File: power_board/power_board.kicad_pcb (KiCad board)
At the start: 2 copper layers, 5 parts, among them Q1 IQD016N08NM5SCATMA1, Q2 IQD016N08NM5SCATMA1, U1 STM32L431KCUx, U2 UCC27282DRCR

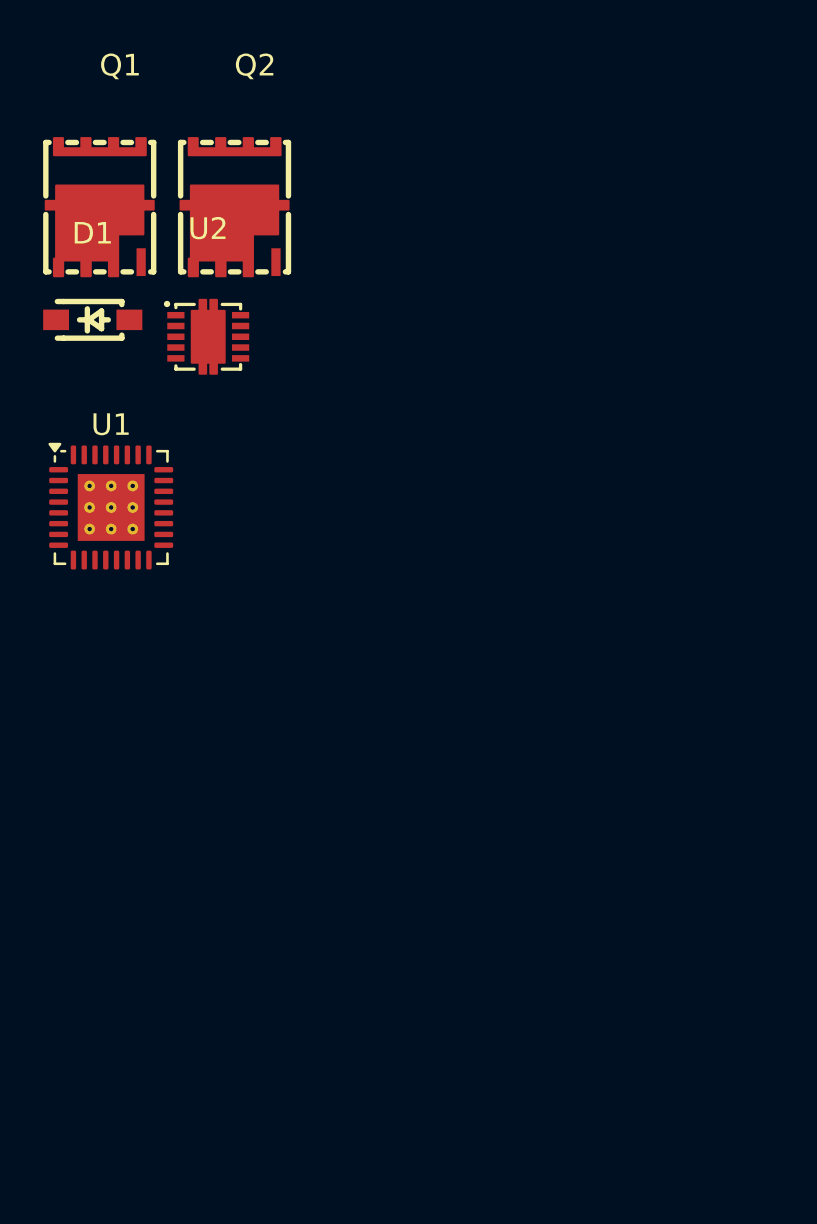
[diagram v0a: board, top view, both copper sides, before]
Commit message: Seperat submodules into split sheets
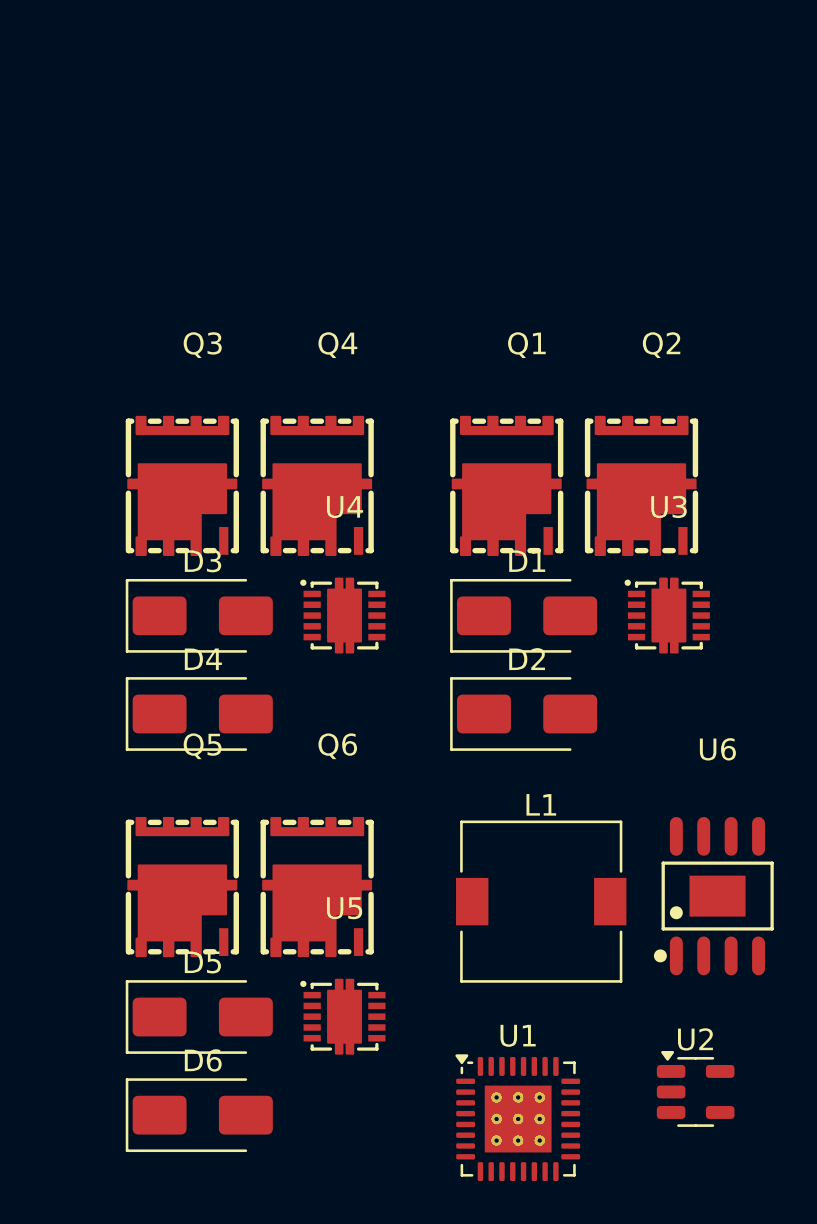
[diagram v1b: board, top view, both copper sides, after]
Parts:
- added D2: SS34, Diode_SMD:D_SMA, F.Cu at (69.5, 63.5)
- added D3: SS34, Diode_SMD:D_SMA, F.Cu at (54.5, 59.0)
- added D4: SS34, Diode_SMD:D_SMA, F.Cu at (54.5, 63.5)
- added D5: SS34, Diode_SMD:D_SMA, F.Cu at (54.5, 77.6)
- added D6: SS34, Diode_SMD:D_SMA, F.Cu at (54.5, 82.1)
- added L1: L_Small, Inductor_SMD:L_7.3x7.3_H4.5, F.Cu at (70.2, 72.2)
- added Q3: IQD016N08NM5SCATMA1, esc-library:PG-TSON-8_L6.0-W5.0_IQD020N10NM5ATMA1, F.Cu at (54.5, 52.9)
- added Q4: IQD016N08NM5SCATMA1, esc-library:PG-TSON-8_L6.0-W5.0_IQD020N10NM5ATMA1, F.Cu at (60.8, 52.9)
- added Q5: IQD016N08NM5SCATMA1, esc-library:PG-TSON-8_L6.0-W5.0_IQD020N10NM5ATMA1, F.Cu at (54.5, 71.5)
- added Q6: IQD016N08NM5SCATMA1, esc-library:PG-TSON-8_L6.0-W5.0_IQD020N10NM5ATMA1, F.Cu at (60.8, 71.5)
- added U3: UCC27282DRCR, esc-library:VSON-10_L3.0-W3.0-P0.50-TL-EP, F.Cu at (76.1, 59.0)
- added U4: UCC27282DRCR, esc-library:VSON-10_L3.0-W3.0-P0.50-TL-EP, F.Cu at (61.1, 59.0)
- added U5: UCC27282DRCR, esc-library:VSON-10_L3.0-W3.0-P0.50-TL-EP, F.Cu at (61.1, 77.6)
- added U6: LM5163DDAR, esc-library:ESOP-8_L4.9-W3.9-P1.27-LS6.0-BL-EP2.6, F.Cu at (78.4, 72.0)
- D1: value BAV19W_C5204748 -> SS34; footprint esc-library:SOD-123_L2.7-W1.6-LS3.7-RD-1 -> Diode_SMD:D_SMA
- U2: value UCC27282DRCR -> INA180A1; footprint esc-library:VSON-10_L3.0-W3.0-P0.50-TL-EP -> Package_TO_SOT_SMD:SOT-23-5
- moved U2 41.7 mm to (77.4, 81.0)
- moved U1 34.1 mm to (69.1, 82.3)
- moved D1 24.4 mm to (69.5, 59.0)
- moved Q1 22.9 mm to (69.6, 52.9)
- moved Q2 22.9 mm to (75.8, 52.9)
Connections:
- net /MOTOR_PHASE_A renamed /half_bridge_0/MOTOR_PHASE
- net /half_bridge0/V_B renamed Net-(D1-K)
- net VBUS renamed /half_bridge_0/VDD
- D1 pad 2: /half_bridge0/VCC -> Net-(D1-A)
- Q1 pad 4: Net-(Q1-G) -> Net-(D1-A)
- Q2 pad 1: GND -> /curret_sense/current+
- U1 pad 1: unconnected-(U1-VDD-Pad1) -> +3V3
- U1 pad 10: unconnected-(U1-PA4-Pad10) -> /mcu/MOTOR_PHASE_FB_B
- U1 pad 11: unconnected-(U1-PA5-Pad11) -> /mcu/MOTOR_PHASE_FB_C
- U1 pad 12: unconnected-(U1-PA6-Pad12) -> /mcu/V_SENSE
- U1 pad 13: unconnected-(U1-PA7-Pad13) -> /half_bridge_2/DRIVER_LOW
- U1 pad 14: unconnected-(U1-PB0-Pad14) -> /half_bridge_1/DRIVER_LOW
- U1 pad 15: unconnected-(U1-PB1-Pad15) -> /half_bridge_0/DRIVER_LOW
- U1 pad 16: Net-(U1-VSS-Pad16) -> GND
- U1 pad 17: unconnected-(U1-VDD-Pad17) -> +3V3
- U1 pad 18: unconnected-(U1-PA8-Pad18) -> /half_bridge_2/DRIVER_HIGH
- U1 pad 19: unconnected-(U1-PA9-Pad19) -> /half_bridge_1/DRIVER_HIGH
- U1 pad 20: unconnected-(U1-PA10-Pad20) -> /half_bridge_0/DRIVER_HIGH
- U1 pad 23: unconnected-(U1-PA13-Pad23) -> /mcu/SWDIO
- U1 pad 24: unconnected-(U1-PA14-Pad24) -> /mcu/SWDCLK
- U1 pad 32: Net-(U1-VSS-Pad16) -> GND
- U1 pad 33: Net-(U1-VSS-Pad16) -> GND
- U1 pad 5: unconnected-(U1-VDDA-Pad5) -> +3V3A
- U1 pad 6: unconnected-(U1-PA0-Pad6) -> /mcu/MOTOR_PHASE_FB_A
- U1 pad 7: unconnected-(U1-PA1-Pad7) -> /mcu/BEMF_REF
- U1 pad 9: unconnected-(U1-PA3-Pad9) -> /curret_sense/I_OUT
- U2 pad 1: unconnected-(U2-VDD-Pad1) -> Net-(R8-Pad1)
- U2 pad 2: unconnected-(U2-NC-Pad2) -> GND
- U2 pad 3: unconnected-(U2-HB-Pad3) -> /curret_sense/current+
- U2 pad 4: unconnected-(U2-HO-Pad4) -> /curret_sense/current-
- U2 pad 5: unconnected-(U2-HS-Pad5) -> +3V3

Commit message: Start multichannel layout
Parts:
- removed U1: STM32L431KCUx, Package_DFN_QFN:QFN-32-1EP_5x5mm_P0.5mm_EP3.1x3.1mm_ThermalVias
- removed U2: INA180A1, Package_TO_SOT_SMD:SOT-23-5
- added C1: 10u, Capacitor_SMD:C_2220_5750Metric, F.Cu at (25.6, 23.7)
- added C10: 100n, Capacitor_SMD:C_0603_1608Metric, F.Cu at (38.4, 69.2)
- added C11: 100n, Capacitor_SMD:C_0603_1608Metric, F.Cu at (42.4, 101.3)
- added C12: 100n, Capacitor_SMD:C_0603_1608Metric, F.Cu at (42.4, 103.8)
- added C13: 1u, Capacitor_SMD:C_0603_1608Metric, F.Cu at (159.4, 81.8)
- added C14: 100n, Capacitor_SMD:C_0603_1608Metric, F.Cu at (159.2, 79.3)
- added C15: 100n, Capacitor_SMD:C_0603_1608Metric, F.Cu at (156.0, 79.3)
- added C16: 1000p, Capacitor_SMD:C_0603_1608Metric, F.Cu at (156.0, 77.7)
- added C17: 1u, Capacitor_SMD:C_0603_1608Metric, F.Cu at (142.7, 81.8)
- added C18: 100n, Capacitor_SMD:C_0603_1608Metric, F.Cu at (142.5, 79.3)
- added C19: 100n, Capacitor_SMD:C_0603_1608Metric, F.Cu at (139.3, 77.7)
- added C2: 10u, Capacitor_SMD:C_2220_5750Metric, F.Cu at (25.6, 30.6)
- added C20: 1000p, Capacitor_SMD:C_0603_1608Metric, F.Cu at (139.3, 79.3)
- added C21: 1u, Capacitor_SMD:C_0603_1608Metric, F.Cu at (175.6, 79.1)
- added C22: 100n, Capacitor_SMD:C_0603_1608Metric, F.Cu at (175.8, 81.6)
- added C23: 100n, Capacitor_SMD:C_0603_1608Metric, F.Cu at (172.4, 77.5)
- added C24: 1000p, Capacitor_SMD:C_0603_1608Metric, F.Cu at (172.4, 79.1)
- added C25: 2.2u, Capacitor_SMD:C_0603_1608Metric, F.Cu at (66.2, 157.8)
- added C26: 1u, Capacitor_SMD:C_0603_1608Metric, F.Cu at (33.3, 138.6)
- added C27: 1u, Capacitor_SMD:C_0603_1608Metric, F.Cu at (32.0, 162.2)
- added C28: 1u, Capacitor_SMD:C_0603_1608Metric, F.Cu at (38.9, 139.0)
- added C29: 1u, Capacitor_SMD:C_0603_1608Metric, F.Cu at (36.6, 160.0)
- added C3: 10u, Capacitor_SMD:C_2220_5750Metric, F.Cu at (25.6, 37.6)
- added C30: 2.2u, Capacitor_SMD:C_0603_1608Metric, F.Cu at (109.1, 154.9)
- added C31: 56p, Capacitor_SMD:C_0603_1608Metric, F.Cu at (83.2, 161.9)
- added C32: 10n, Capacitor_SMD:C_0603_1608Metric, F.Cu at (47.9, 139.3)
- added C33: 10n, Capacitor_SMD:C_0603_1608Metric, F.Cu at (46.5, 166.8)
- added C34: 3.3n, Capacitor_SMD:C_0603_1608Metric, F.Cu at (83.2, 164.4)
- added C35: 22u, Capacitor_SMD:C_0603_1608Metric, F.Cu at (109.1, 162.4)
- added C36: 2.2u, Capacitor_SMD:C_0603_1608Metric, F.Cu at (47.9, 141.8)
- added C37: 2.2u, Capacitor_SMD:C_0603_1608Metric, F.Cu at (47.9, 163.2)
- added C4: 10u, Capacitor_SMD:C_2220_5750Metric, F.Cu at (25.6, 44.5)
- added C5: 100n, Capacitor_SMD:C_0603_1608Metric, F.Cu at (38.4, 66.2)
- added C6: 100n, Capacitor_SMD:C_0603_1608Metric, F.Cu at (38.4, 70.8)
- added C7: 100n, Capacitor_SMD:C_0603_1608Metric, F.Cu at (38.4, 67.7)
- added C8: 10u, Capacitor_SMD:C_0603_1608Metric, F.Cu at (38.4, 72.4)
- added C9: 100n, Capacitor_SMD:C_0603_1608Metric, F.Cu at (49.4, 72.4)
- added D7: LED, LED_SMD:LED_0603_1608Metric, F.Cu at (99.6, 161.4)
- added R1: 1k, Resistor_SMD:R_0603_1608Metric, F.Cu at (45.0, 64.1)
- added R10: 4.7, Resistor_SMD:R_0603_1608Metric, F.Cu at (156.8, 86.6)
- added R11: 4.7, Resistor_SMD:R_0603_1608Metric, F.Cu at (157.0, 75.0)
- added R12: 10, Resistor_SMD:R_0603_1608Metric, F.Cu at (155.0, 86.6)
- added R13: 10, Resistor_SMD:R_0603_1608Metric, F.Cu at (155.4, 75.0)
- added R14: 100k, Resistor_SMD:R_0603_1608Metric, F.Cu at (154.8, 91.4)
- added R15: 100k, Resistor_SMD:R_0603_1608Metric, F.Cu at (155.0, 71.6)
- added R16: 10k, Resistor_SMD:R_0603_1608Metric, F.Cu at (147.4, 85.2)
- added R17: 1k, Resistor_SMD:R_0603_1608Metric, F.Cu at (147.4, 89.2)
- added R18: 4.7, Resistor_SMD:R_0603_1608Metric, F.Cu at (140.1, 86.6)
- added R19: 4.7, Resistor_SMD:R_0603_1608Metric, F.Cu at (140.3, 75.0)
- added R2: 10k, Resistor_SMD:R_0603_1608Metric, F.Cu at (42.5, 64.1)
- added R20: 10, Resistor_SMD:R_0603_1608Metric, F.Cu at (138.3, 86.6)
- added R21: 10, Resistor_SMD:R_0603_1608Metric, F.Cu at (138.7, 75.0)
- added R22: 100k, Resistor_SMD:R_0603_1608Metric, F.Cu at (138.1, 91.4)
- added R23: 100k, Resistor_SMD:R_0603_1608Metric, F.Cu at (138.3, 71.6)
- added R24: 10k, Resistor_SMD:R_0603_1608Metric, F.Cu at (130.7, 85.2)
- added R25: 1k, Resistor_SMD:R_0603_1608Metric, F.Cu at (130.7, 89.2)
- added R26: 4.7, Resistor_SMD:R_0603_1608Metric, F.Cu at (173.2, 86.4)
- added R27: 4.7, Resistor_SMD:R_0603_1608Metric, F.Cu at (173.4, 74.8)
- added R28: 10, Resistor_SMD:R_0603_1608Metric, F.Cu at (171.4, 86.4)
- added R29: 10, Resistor_SMD:R_0603_1608Metric, F.Cu at (171.8, 74.8)
- added R3: 100k, Resistor_SMD:R_0603_1608Metric, F.Cu at (27.5, 79.5)
- added R30: 100k, Resistor_SMD:R_0603_1608Metric, F.Cu at (171.2, 91.2)
- added R31: 100k, Resistor_SMD:R_0603_1608Metric, F.Cu at (171.4, 71.4)
- added R32: 10k, Resistor_SMD:R_0603_1608Metric, F.Cu at (163.8, 85.0)
- added R33: 1k, Resistor_SMD:R_0603_1608Metric, F.Cu at (163.8, 89.0)
- added R34: 2.2, Resistor_SMD:R_0603_1608Metric, F.Cu at (33.2, 140.4)
- added R35: 1, Resistor_SMD:R_0603_1608Metric, F.Cu at (31.4, 159.8)
- added R36: R_Small, Resistor_SMD:R_0603_1608Metric, F.Cu at (66.2, 161.6)
- added R37: 226k, Resistor_SMD:R_0603_1608Metric, F.Cu at (87.2, 162.4)
- added R38: 453k, Resistor_SMD:R_0603_1608Metric, F.Cu at (78.5, 162.0)
- added R39: 49.9, Resistor_SMD:R_0603_1608Metric, F.Cu at (78.5, 164.5)
- added R4: 5k, Resistor_SMD:R_0603_1608Metric, F.Cu at (27.5, 82.0)
- added R40: 2.2k, Resistor_SMD:R_0603_1608Metric, F.Cu at (95.4, 162.3)
- added R5: 10k, Resistor_SMD:R_0603_1608Metric, F.Cu at (36.5, 80.0)
- added R6: 10k, Resistor_SMD:R_0603_1608Metric, F.Cu at (36.5, 82.5)
- added R7: 10k, Resistor_SMD:R_0603_1608Metric, F.Cu at (36.5, 85.5)
- added R8: 0.001, Resistor_SMD:R_0603_1608Metric, F.Cu at (42.4, 106.3)
- added R9: 1k, Resistor_SMD:R_0603_1608Metric, F.Cu at (42.4, 108.8)
- added U10: 66565S0M3, esc-library:CONN-SMD_66565S0M3, F.Cu at (166.8, 77.8)
- added U11: LM5163DDAR, esc-library:ESOP-8_L4.9-W3.9-P1.27-LS6.0-BL-EP2.6, F.Cu at (72.9, 157.8)
- added U12: LP2985-33DBVR, esc-library:SOT-23-5_L3.0-W1.7-P0.95-LS2.8-BR, F.Cu at (42.8, 139.3)
- added U13: LP2985-33DBVR, esc-library:SOT-23-5_L3.0-W1.7-P0.95-LS2.8-BR, F.Cu at (42.4, 160.7)
- added U7: UCC27282DRCR, esc-library:VSON-10_L3.0-W3.0-P0.50-TL-EP, F.Cu at (139.9, 82.5)
- added U8: 66565S0M3, esc-library:CONN-SMD_66565S0M3, F.Cu at (133.7, 78.0)
- added U9: UCC27282DRCR, esc-library:VSON-10_L3.0-W3.0-P0.50-TL-EP, F.Cu at (173.0, 82.3)
- D1, D2, D3, D4, D5, D6: value SS34 -> B5819WS_C7420331; footprint Diode_SMD:D_SMA -> esc-library:SOD-323_L1.7-W1.3-LS2.5-FD
- Q1, Q2, Q3, Q4, Q5, Q6: value IQD016N08NM5SCATMA1 -> BSC0702LS; footprint esc-library:PG-TSON-8_L6.0-W5.0_IQD020N10NM5ATMA1 -> esc-library:PG-TDSON-8_L5.0-W6.0-P1.27-BL-EP
- U3: value UCC27282DRCR -> STM32L431KCUx; footprint esc-library:VSON-10_L3.0-W3.0-P0.50-TL-EP -> Package_DFN_QFN:QFN-32-1EP_5x5mm_P0.5mm_EP3.1x3.1mm_ThermalVias
- U4: value UCC27282DRCR -> INA180A1; footprint esc-library:VSON-10_L3.0-W3.0-P0.50-TL-EP -> Package_TO_SOT_SMD:SOT-23-5
- U6: value LM5163DDAR -> 66565S0M3; footprint esc-library:ESOP-8_L4.9-W3.9-P1.27-LS6.0-BL-EP2.6 -> esc-library:CONN-SMD_66565S0M3
- moved D6 119.4 mm to (173.4, 71.4), turned to -90 degrees
- moved D5 119.3 mm to (173.2, 89.6), turned to 90 degrees
- moved Q5 112.4 mm to (166.9, 67.6)
- moved Q6 108.1 mm to (167.7, 87.6)
- moved U5 95.6 mm to (156.6, 82.5), turned to -90 degrees
- moved D1 92.5 mm to (156.8, 89.8), turned to 90 degrees
- moved D3 91.0 mm to (140.1, 89.8), turned to 90 degrees
- moved D2 87.8 mm to (157.0, 71.6), turned to -90 degrees
- moved D4 86.2 mm to (140.3, 71.6), turned to -90 degrees
- moved Q2 83.1 mm to (151.3, 87.8)
- moved Q1 82.3 mm to (150.5, 67.8)
- moved Q4 81.6 mm to (134.6, 87.8)
- moved Q3 80.6 mm to (133.8, 67.8)
- moved L1 79.0 mm to (85.0, 149.8)
- moved U6 72.3 mm to (150.4, 78.0), turned to 90 degrees
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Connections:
- D1 pad 1: Net-(D1-K) -> Net-(D1-A)
- D1 pad 2: Net-(D1-A) -> Net-(D1-K)
- D2 pad 1: Net-(D2-K) -> Net-(D2-A)
- D2 pad 2: Net-(D2-A) -> Net-(D2-K)
- D3 pad 1: Net-(D3-K) -> Net-(D3-A)
- D3 pad 2: Net-(D3-A) -> Net-(D3-K)
- D4 pad 1: Net-(D4-K) -> Net-(D4-A)
- D4 pad 2: Net-(D4-A) -> Net-(D4-K)
- D5 pad 1: Net-(D5-K) -> Net-(D5-A)
- D5 pad 2: Net-(D5-A) -> Net-(D5-K)
- D6 pad 1: Net-(D6-K) -> Net-(D6-A)
- D6 pad 2: Net-(D6-A) -> Net-(D6-K)
- L1 pad 1: Net-(U6-BST) -> Net-(U11-BST)
- Q1 pad 4: Net-(D1-A) -> Net-(D2-A)
- Q1 pad 5: /half_bridge_0/VDD -> VBUS
- Q2 pad 4: Net-(D2-A) -> Net-(D1-A)
- Q3 pad 4: Net-(D3-A) -> Net-(D4-A)
- Q3 pad 5: /half_bridge_1/VDD -> VBUS
- Q4 pad 4: Net-(D4-A) -> Net-(D3-A)
- Q5 pad 4: Net-(D5-A) -> Net-(D6-A)
- Q5 pad 5: /half_bridge_2/VDD -> VBUS
- Q6 pad 4: Net-(D6-A) -> Net-(D5-A)
- U3 pad 1: +12V -> +3V3
- U3 pad 10: /half_bridge_0/DRIVER_LO -> /mcu/MOTOR_PHASE_FB_B
- U3 pad 11: GNDPWR -> /mcu/MOTOR_PHASE_FB_C
- U3 pad 3: Net-(U3-HB) -> unconnected-(U3-PC15-Pad3)
- U3 pad 4: /half_bridge_0/DRIVER_HO -> Net-(U3-NRST)
- U3 pad 5: /half_bridge_0/MOTOR_PHASE -> +3V3A
- U3 pad 6: Net-(U3-EN) -> /mcu/MOTOR_PHASE_FB_A
- U3 pad 7: /half_bridge_0/DRIVER_HIGH -> /mcu/BEMF_REF
- U3 pad 8: /half_bridge_0/DRIVER_LOW -> unconnected-(U3-PA2-Pad8)
- U3 pad 9: GNDPWR -> /curret_sense/I_OUT
- U4 pad 1: +12V -> Net-(R9-Pad1)
- U4 pad 2: unconnected-(U4-NC-Pad2) -> GND
- U4 pad 3: Net-(U4-HB) -> /curret_sense/current+
- U4 pad 4: /half_bridge_1/DRIVER_HO -> GNDPWR
- U4 pad 5: /half_bridge_1/MOTOR_PHASE -> +3V3A
- U5 pad 10: /half_bridge_2/DRIVER_LO -> /half_bridge_0/DRIVER_LO
- U5 pad 4: /half_bridge_2/DRIVER_HO -> /half_bridge_0/DRIVER_HO
- U5 pad 5: /half_bridge_2/MOTOR_PHASE -> /half_bridge_0/MOTOR_PHASE
- U5 pad 6: Net-(U5-EN) -> +12V
- U5 pad 7: /half_bridge_2/DRIVER_HIGH -> /half_bridge_0/DRIVER_HIGH
- U5 pad 8: /half_bridge_2/DRIVER_LOW -> /half_bridge_0/DRIVER_LOW
- U6 pad 1: GND -> /half_bridge_0/MOTOR_PHASE
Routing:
- net GNDPWR: track 0.00 -> 43.2 mm, vias 0 -> 18
- net +12V: track 0.00 -> 12.8 mm, vias 0 -> 3
- net /curret_sense/current+: track 0.00 -> 11.1 mm
- net /half_bridge_1/MOTOR_PHASE: track 0.00 -> 8.66 mm
- net /half_bridge_0/MOTOR_PHASE: track 0.00 -> 8.66 mm
- net /half_bridge_2/MOTOR_PHASE: track 0.00 -> 8.66 mm
- net Net-(D4-A): track 0.00 -> 8.59 mm
- net Net-(D2-A): track 0.00 -> 8.59 mm
- net Net-(D6-A): track 0.00 -> 8.59 mm
- net /half_bridge_1/DRIVER_HO: track 0.00 -> 7.09 mm
- net /half_bridge_0/DRIVER_HO: track 0.00 -> 7.09 mm
- net /half_bridge_2/DRIVER_HO: track 0.00 -> 7.09 mm
- net Net-(D1-A): track 0.00 -> 6.97 mm
- net Net-(D5-A): track 0.00 -> 6.97 mm
- net Net-(D3-A): track 0.00 -> 6.97 mm
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- added copper zone on F.Cu, net /half_bridge_2/MOTOR_PHASE

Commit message: Complete primary layout step
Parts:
- removed the C1 at (25.6, 23.7)
- removed the C2 at (25.6, 30.6)
- removed the C3 at (25.6, 37.6)
- removed the C4 at (25.6, 44.5)
- added C13: 10u, Capacitor_SMD:C_1210_3225Metric, F.Cu at (60.3, 52.8)
- added C18: 10u, Capacitor_SMD:C_1210_3225Metric, F.Cu at (80.5, 52.8)
- added C23: 10u, Capacitor_SMD:C_1210_3225Metric, F.Cu at (100.7, 52.7)
- added C37: ERS1KM101G16OT, esc-library:CAP-TH_BD10.0-P5.00-D1.0-FD, F.Cu at (49.0, 54.8)
- added C38: ERS1KM101G16OT, esc-library:CAP-TH_BD10.0-P5.00-D1.0-FD, F.Cu at (49.1, 66.8)
- added C39: 1u, Capacitor_SMD:C_0603_1608Metric, F.Cu at (35.4, 99.8)
- added C40: 1u, Capacitor_SMD:C_0603_1608Metric, F.Cu at (39.4, 99.8)
- added C41: 10n, Capacitor_SMD:C_0603_1608Metric, F.Cu at (28.2, 98.6)
- added C42: 2.2u, Capacitor_SMD:C_0603_1608Metric, F.Cu at (28.2, 100.6)
- added CN1: XT90PW-M.G.Y, esc-library:CONN-TH_XT90PW-M.G.Y, F.Cu at (40.5, 32.3)
- added CN2: XT60PW-M, esc-library:CONN-TH_XT60PW-M, F.Cu at (33.8, 32.3)
- added R41: 2.2, Resistor_SMD:R_0603_1608Metric, F.Cu at (42.0, 101.0)
- added U12: LP2985-33DBVR, esc-library:SOT-23-5_L3.0-W1.7-P0.95-LS2.8-BR, F.Cu at (32.1, 99.6)
- C34: renamed from C35; footprint Capacitor_SMD:C_0603_1608Metric -> Capacitor_SMD:C_1210_3225Metric
- R36: value R_Small -> 100k
- R39: value 49.9 -> 49.9k
- R8: value 0.001 -> HOVB4026-5W-0.5MR-1%; footprint Resistor_SMD:R_0603_1608Metric -> esc-library:RES-SMD_4P-L10.8-W6.7
- moved C34 96.8 mm to (56.6, 81.0), turned to 180 degrees
- moved C29 87.5 mm to (52.4, 88.2), turned to 180 degrees
- moved C9 86.1 mm to (75.0, 64.4)
- moved D1 86.1 mm to (72.4, 72.4)
- moved Q1 86.1 mm to (66.1, 50.3)
- moved R10 86.1 mm to (72.4, 69.2)
- moved R13 86.1 mm to (71.0, 57.5)
- moved R14 86.1 mm to (70.4, 74.0)
- moved R16 86.1 mm to (63.0, 67.7)
- moved R17 86.1 mm to (63.0, 71.8)
- moved U4 86.1 mm to (66.0, 60.5)
- moved C10 86.1 mm to (74.8, 61.8)
- moved C11 86.1 mm to (71.6, 61.8)
- moved C12 86.1 mm to (71.6, 60.2)
- moved D2 86.1 mm to (72.6, 54.2)
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- renumbered C5 to C1, C14 to C10, C15 to C11, C16 to C12, C17 to C14, C18 to C15, C19 to C16, C20 to C17, C21 to C19, C6 to C2, C22 to C20, C23 to C21, C24 to C22, C25 to C24, C26 to C25, C27 to C26, C28 to C27, C29 to C28, C30 to C29, C7 to C3, C31 to C30, C32 to C31, C33 to C32, C34 to C33, C36 to C35, C37 to C36, C8 to C4, C9 to C5, C10 to C6, C11 to C7, C12 to C8, C13 to C9, U3 to U1, U12 to U10, U13 to U11, U4 to U2, U5 to U3, U6 to U4, U7 to U5, U8 to U6, U9 to U7, U10 to U8, U11 to U9
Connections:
- C29 pad 1: Net-(U11-SW) -> Net-(U9-SW)
- C29 pad 2: Net-(U11-BST) -> Net-(U9-BST)
- C7 pad 1: +3V3A -> +3V3A0
- L1 pad 1: Net-(U11-BST) -> Net-(U9-SW)
- R37 pad 2: Net-(U11-BST) -> Net-(U9-SW)
- R8 pad 1: /curret_sense/current+ -> GNDPWR
- R8 pad 2: GNDPWR -> /curret_sense/current+
- U2 pad 3: /curret_sense/current+ -> Net-(U2-+)
- U2 pad 4: GNDPWR -> Net-(U2--)
- U2 pad 5: +3V3A -> +3V3A0
- U9 pad 7: Net-(U11-BST) -> Net-(U9-BST)
- U9 pad 8: Net-(U11-SW) -> Net-(U9-SW)
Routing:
- added copper zone on F.Cu, net /half_bridge_0/MOTOR_PHASE
- added copper zone on F.Cu, net /half_bridge_1/MOTOR_PHASE
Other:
- board outline added: 100 x 100 mm

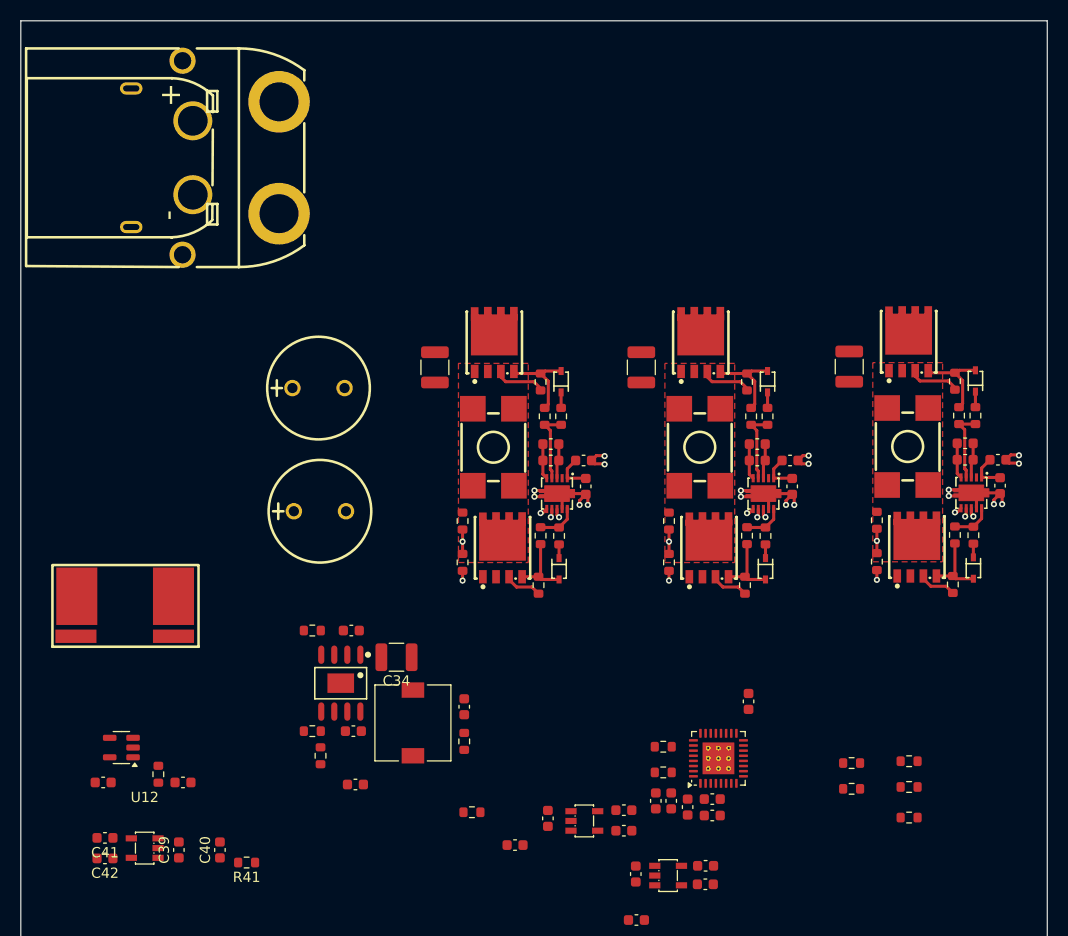
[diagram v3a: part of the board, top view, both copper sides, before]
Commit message: Phase control signal layout
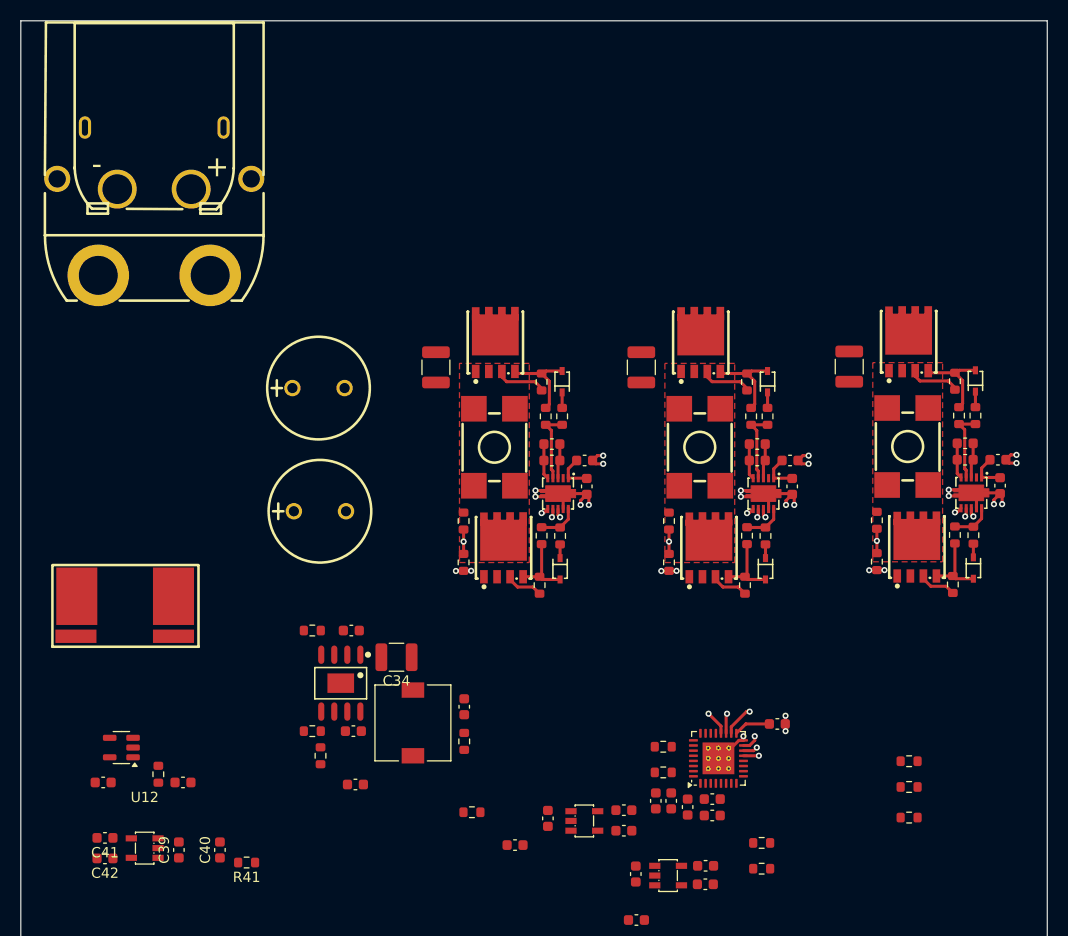
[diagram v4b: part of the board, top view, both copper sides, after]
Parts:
- moved R3 11.7 mm to (92.2, 99.1)
- moved R4 11.7 mm to (92.2, 101.6)
- moved CN1 10.1 mm to (33.0, 39.1), turned to 0 degrees
- moved C5 3.56 mm to (93.7, 87.5), turned to 0 degrees
- moved CN2 0.76 mm to (33.0, 32.4), turned to -90 degrees
- moved C9 0.10 mm to (75.1, 64.4)
- moved Q1 0.10 mm to (66.2, 50.3)
- moved Q2 0.10 mm to (67.0, 70.3)
- moved R13 0.10 mm to (71.1, 57.5)
- moved U3 0.10 mm to (72.3, 65.1)
- moved U4 0.10 mm to (66.1, 60.5)
- moved C13 0.10 mm to (60.4, 52.8)
- moved R16 0.10 mm to (63.1, 67.7)
- moved R17 0.10 mm to (63.1, 71.8)
- moved C10 0.10 mm to (74.9, 61.8)
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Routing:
- net /half_bridge_2/DRIVER_LOW: track 0.88 -> 45.6 mm, vias 1 -> 2
- net /half_bridge_2/DRIVER_HIGH: track 0.84 -> 42.4 mm, vias 1 -> 2
- net /half_bridge_0/DRIVER_LOW: track 0.88 -> 32.6 mm, vias 1 -> 2
- net /half_bridge_1/DRIVER_LOW: track 0.88 -> 29.8 mm, vias 1 -> 2
- net /half_bridge_0/DRIVER_HIGH: track 0.84 -> 28.8 mm, vias 1 -> 2
- net /half_bridge_1/DRIVER_HIGH: track 0.84 -> 25.7 mm, vias 1 -> 2
- net GND: track 2.85 -> 9.64 mm, vias 3 -> 9
- net +3V3: track 0.00 -> 3.59 mm
- added copper zone on In1.Cu, net GND
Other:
- copper layers 2 -> 4
